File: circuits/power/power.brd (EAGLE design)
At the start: 36.8 x 25.9 mm, 22 parts

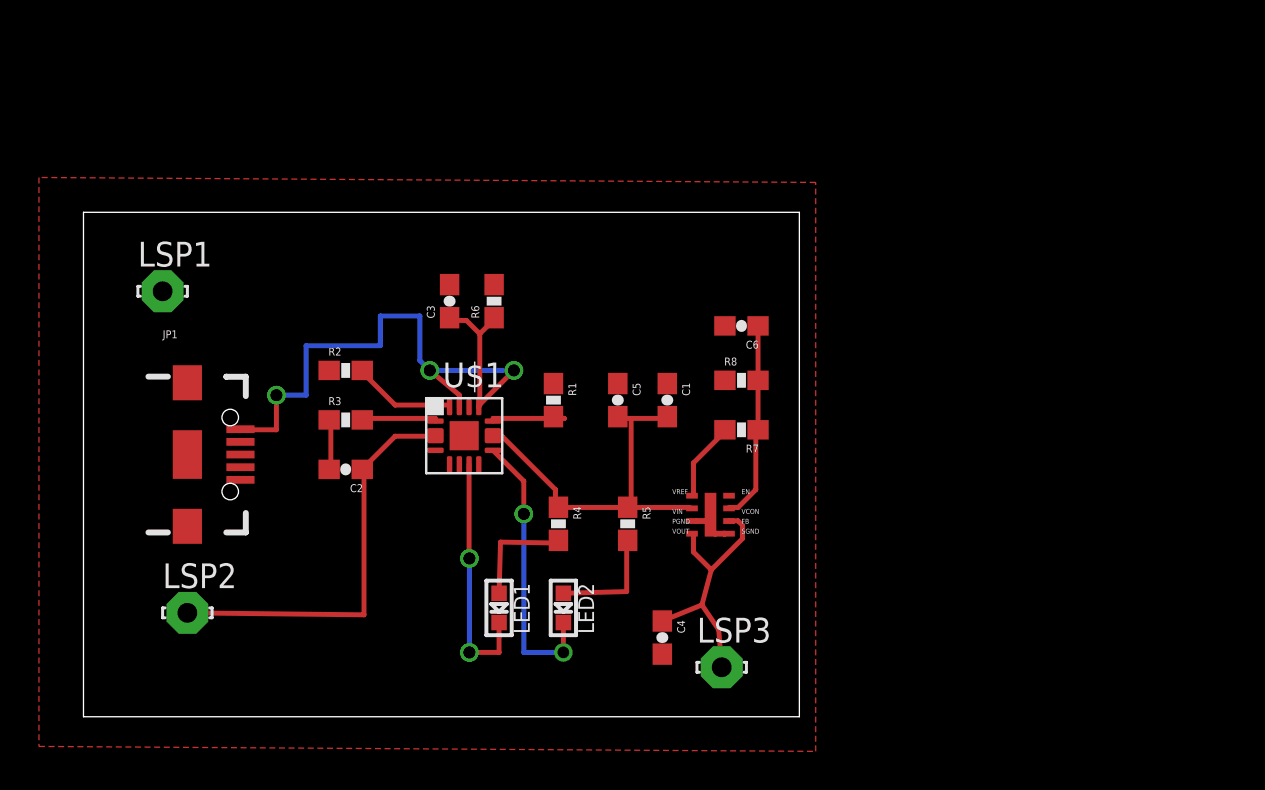
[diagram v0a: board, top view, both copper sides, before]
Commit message: changed LMZ10500 library. updated power schematic and switched out usb. Made new power layout.
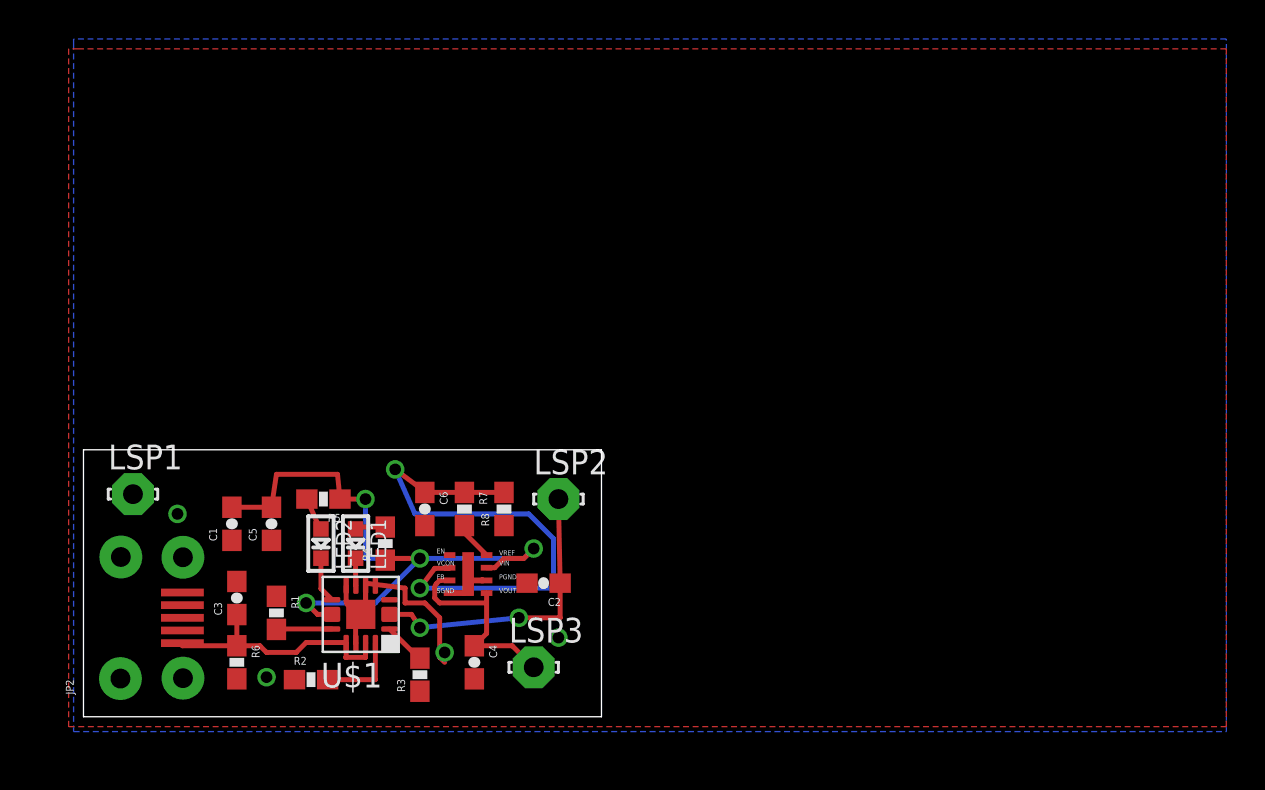
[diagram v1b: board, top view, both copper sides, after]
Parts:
- removed JP1: (no value), SparkFun-Connectors:USB-B-MICRO-SMD_V03
- added JP2: (no value), SparkFun-Connectors:MICRO-B-SMT
- moved C1 23.2 mm to (7.62, 9.91), turned to 90 degrees
- moved R6 22.8 mm to (7.87, 2.79), turned to 270 degrees
- moved LSP2 19.9 mm to (24.4, 11.2)
- moved C5 18.9 mm to (9.65, 9.91), turned to 90 degrees
- moved C6 18.8 mm to (17.5, 10.7), turned to 270 degrees
- moved C3 18.7 mm to (7.87, 6.10)
- moved R1 17.9 mm to (9.91, 5.33)
- moved R2 16.0 mm to (11.7, 1.91)
- moved R5 15.7 mm to (12.3, 11.2), turned to 180 degrees
- moved R7 14.8 mm to (19.6, 10.7), turned to 270 degrees
- moved R8 13.9 mm to (21.6, 10.7), turned to 90 degrees
- moved R3 13.6 mm to (17.3, 2.16), turned to 90 degrees
- moved LED2 12.9 mm to (12.2, 8.89)
- moved U$2 12.8 mm to (18.8, 6.35)
- moved C2 11.7 mm to (23.6, 6.86)
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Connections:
- removed net N$25: U$2.SGND
- removed net N$8: C1.1, C2.2, C3.2, C4.2, C5.1, C6.2, JP1.GND1, LSP1.MP, R1.1, R2.1, R3.1, R6.2, R8.1, U$1.14, U$1.4, U$1.5, U$1.6, U$1.8, U$2.PGND
- new net GND: C1.1, C2.2, C3.2, C4.2, C5.1, C6.2, JP2.5, LSP1.MP, R1.1, R2.1, R3.1, R6.2, R8.1, U$1.14, U$1.4, U$1.5, U$1.6, U$1.8, U$2.PGND, U$2.SGND
- net N$14: now also JP2.1; no longer JP1.VBUS1
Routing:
- net N$14: track 34.4 -> 13.0 mm, vias 3 -> 0
- net N$2: track 10.5 -> 27.6 mm, vias 0 -> 2
- net N$9: track 19.5 -> 34.4 mm, vias 0 -> 4
- net GND: track 0.00 -> 13.5 mm, vias 0 -> 4
- net N$12: track 14.6 -> 2.37 mm, vias 2 -> 0
- net N$13: track 12.7 -> 1.42 mm, vias 2 -> 0
- net BAT: track 21.1 -> 15.3 mm, vias 0 -> 2
- net N$10: track 5.84 -> 1.62 mm
- net N$11: track 5.89 -> 1.71 mm
- net VOUT: track 13.6 -> 10.7 mm
- net N$19: track 2.54 -> 0.00 mm
- net N$1: track 4.08 -> 1.99 mm
- net N$6: track 3.91 -> 2.16 mm
- net N$3: track 4.36 -> 2.86 mm
- net N$5: track 5.32 -> 4.33 mm
- added copper zone on layer 1, net GND
- added copper zone on layer 16, net GND
- removed copper zone on layer 1, net N$8
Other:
- board size 36.8 x 25.9 mm -> 26.6 x 13.7 mm
